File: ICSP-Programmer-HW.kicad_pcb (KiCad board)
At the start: 2 copper layers, 45 x 21 mm, 28 parts, among them J1 USB4105-GF-A-060, J2 61200621621, J3 Pins_2.54_1x2, U1 ATMEGA8A-MU, U2 FT230XQ, U3 74LVC1T45Z6, U4 74LVC1T45Z6, U5 74LVC1T45Z6, U6 74LVC1T45Z6, Y1 CSTNE16M0V530000R0

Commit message: Update readme
Add jumper to tie 5V to VCC
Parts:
- added JP1: SolderJumper2, Jumper:SolderJumper-2_P1.3mm_Open_RoundedPad1.0x1.5mm, F.Cu at (114.1, 120.9)
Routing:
- net /Target/TARGET_VCC: track 19.8 -> 40.5 mm
- net +5V: track 69.1 -> 71.3 mm
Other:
- board text added: "VCC"
- board text removed: "V+"

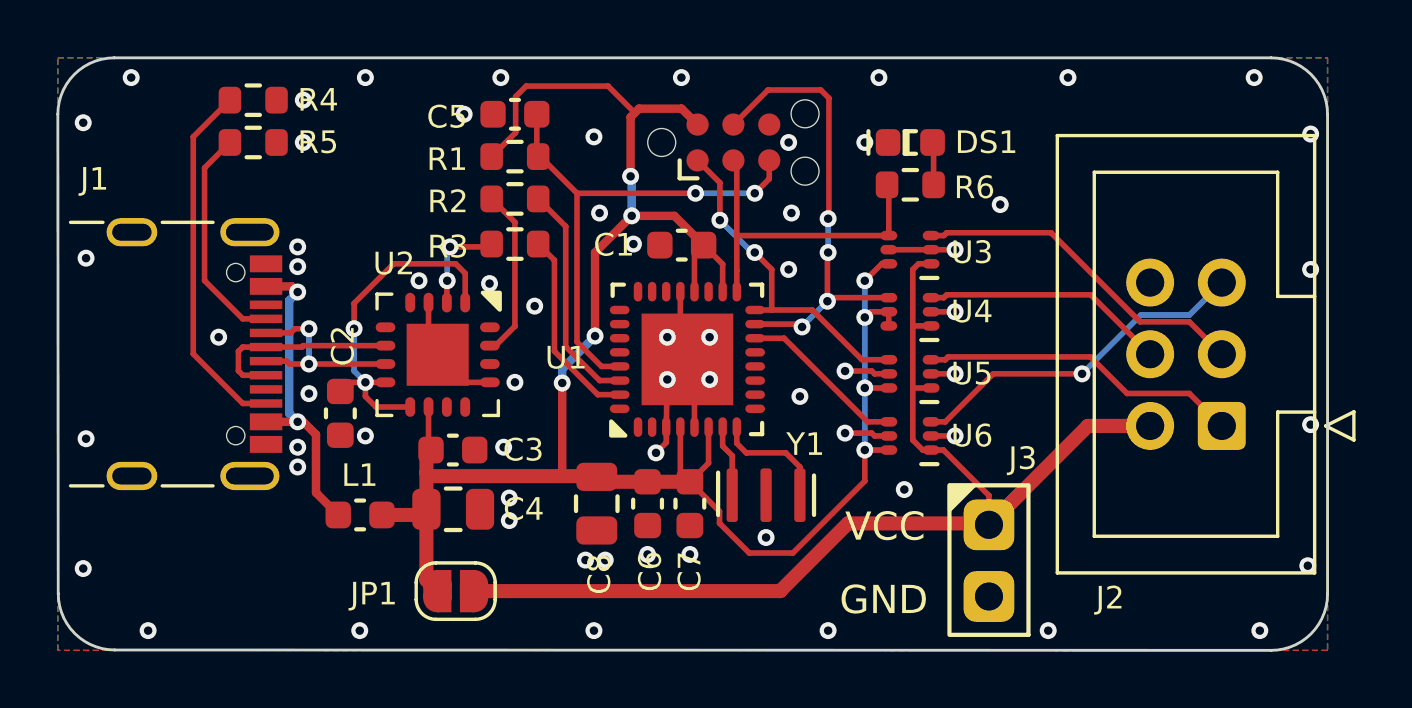
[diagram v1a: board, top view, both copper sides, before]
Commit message: Fix direction issue on MISO/MOSI
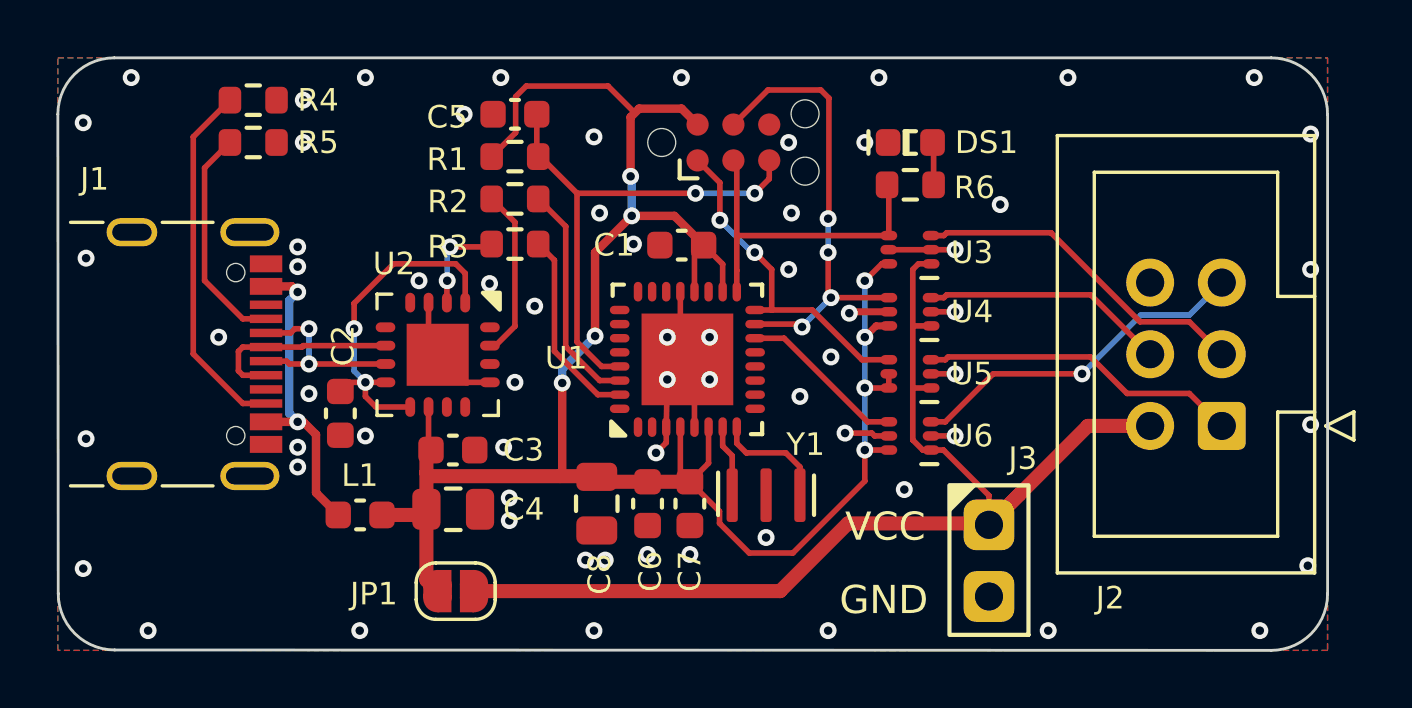
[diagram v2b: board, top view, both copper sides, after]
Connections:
- U4 pad 5: +5V -> GND
- U5 pad 5: GND -> +5V
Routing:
- net GND: track 16.7 -> 16.5 mm, vias 64 -> 65
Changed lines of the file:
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@@
       (net 20 "/MCU/ICSP_MOSI") (pinfunction "B") (pintype "bidirectional"))
     (pad "5" smd oval (at 0.75 0 180) (size 0.6 0.34) (layers "F.Cu" "F.Paste" "F.Mask")
-      (net 1 "+5V") (pinfunction "DIR") (pintype "input"))
+      (net 2 "GND") (pinfunction "DIR") (pintype "input"))
     (pad "6" smd oval (at 0.75 -0.5 180) (size 0.6 0.34) (layers "F.Cu" "F.Paste" "F.Mask")
       (net 1 "+5V") (pinfunction "VCCB") (pintype "power_in"))
@@
       (net 18 "/MCU/ICSP_MISO") (pinfunction "B") (pintype "bidirectional"))
     (pad "5" smd oval (at 0.75 0 180) (size 0.6 0.34) (layers "F.Cu" "F.Paste" "F.Mask")
-      (net 2 "GND") (pinfunction "DIR") (pintype "input"))
+      (net 1 "+5V") (pinfunction "DIR") (pintype "input"))
     (pad "6" smd oval (at 0.75 -0.5 180) (size 0.6 0.34) (layers "F.Cu" "F.Paste" "F.Mask")
       (net 1 "+5V") (pinfunction "VCCB") (pintype "power_in"))
@@
   (segment (start 123.45 118.075) (end 122.4 117.025) (width 0.2) (layer "F.Cu") (net 1))
   (segment (start 113.0625 118) (end 113.0625 116.7) (width 0.5) (layer "F.Cu") (net 1))
+  (segment (start 129.45 111.5) (end 128.999901 111.5) (width 0.25) (layer "F.Cu") (net 1))
   (segment (start 122.5625 110.2875) (end 122.5625 108.9625) (width 0.2) (layer "F.Cu") (net 1))
   (segment (start 128.6 115.9) (end 128.6 117) (width 0.2) (layer "F.Cu") (net 1))
@@
   (segment (start 124.505025 119.55) (end 123.45 118.494975) (width 0.2) (layer "F.Cu") (net 1))
   (segment (start 128.6 115.9) (end 129.45 115.9) (width 0.2) (layer "F.Cu") (net 1))
-  (segment (start 129.45 111) (end 129.45 111.5) (width 0.2) (layer "F.Cu") (net 1))
+  (segment (start 128.999901 111.5) (end 128.599901 111.9) (width 0.25) (layer "F.Cu") (net 1))
+  (segment (start 129.45 113.7) (end 129.45 113.2) (width 0.2) (layer "F.Cu") (net 1))
   (segment (start 126.05 119.55) (end 124.505025 119.55) (width 0.2) (layer "F.Cu") (net 1))
-  (segment (start 128.8 111) (end 128.6 111.2) (width 0.2) (layer "F.Cu") (net 1))
   (segment (start 123.5625 109.3125) (end 122.8875 108.6375) (width 0.2) (layer "F.Cu") (net 1))
   (segment (start 119.039597 108.899742) (end 120.339339 107.6) (width 0.3) (layer "F.Cu") (net 1))
@@
   (segment (start 120.6 103.8) (end 122.1075 103.8) (width 0.3) (layer "F.Cu") (net 1))
   (segment (start 111.4875 118.2) (end 112.8625 118.2) (width 0.5) (layer "F.Cu") (net 1))
-  (segment (start 129.45 111) (end 128.8 111) (width 0.2) (layer "F.Cu") (net 1))
   (segment (start 120.3 104.1) (end 120.6 103.8) (width 0.3) (layer "F.Cu") (net 1))
   (segment (start 123.5625 110.2875) (end 123.5625 109.3125) (width 0.2) (layer "F.Cu") (net 1))
@@
   (via (at 120.3 106.2) (size 0.6) (drill 0.3) (layers "F.Cu" "B.Cu") (net 1))
   (via (at 128.6 115.9) (size 0.6) (drill 0.3) (layers "F.Cu" "B.Cu") (net 1))
-  (via (at 128.6 111.2) (size 0.6) (drill 0.3) (layers "F.Cu" "B.Cu") (net 1))
+  (via (at 128.599901 111.9) (size 0.6) (drill 0.3) (layers "F.Cu" "B.Cu") (net 1))
   (via (at 128.599901 113.7) (size 0.6) (drill 0.3) (layers "F.Cu" "B.Cu") (net 1))
-  (segment (start 128.599901 113.7) (end 128.599901 111.200099) (width 0.2) (layer "B.Cu") (net 1))
+  (segment (start 128.6 111.899901) (end 128.6 109.9005) (width 0.2) (layer "B.Cu") (net 1))
+  (segment (start 128.599901 111.9) (end 128.6 111.899901) (width 0.2) (layer "B.Cu") (net 1))
   (segment (start 117.876089 113.023911) (end 119.039597 111.860403) (width 0.3) (layer "B.Cu") (net 1))
   (segment (start 117.876089 113.523911) (end 117.876089 113.023911) (width 0.3) (layer "B.Cu") (net 1))
+  (segment (start 128.599901 111.9) (end 128.599901 113.7) (width 0.2) (layer "B.Cu") (net 1))
   (segment (start 120.339339 107.6) (end 120.339339 106.239339) (width 0.3) (layer "B.Cu") (net 1))
   (segment (start 120.339339 106.239339) (end 120.3 106.2) (width 0.5) (layer "B.Cu") (net 1))
-  (segment (start 128.599901 111.200099) (end 128.6 111.2) (width 0.2) (layer "B.Cu") (net 1))
   (segment (start 128.599901 113.7) (end 128.599901 115.899901) (width 0.2) (layer "B.Cu") (net 1))
-  (segment (start 128.6 109.9005) (end 128.6 111.2) (width 0.2) (layer "B.Cu") (net 1))
   (segment (start 128.599901 115.899901) (end 128.6 115.9) (width 0.2) (layer "B.Cu") (net 1))
   (segment (start 122.0625 111.3125) (end 121.5 111.875) (width 0.2) (layer "F.Cu") (net 2))
   (segment (start 129.45 115.4) (end 128.948529 115.4) (width 0.2) (layer "F.Cu") (net 2))
   (segment (start 128.948529 115.4) (end 128.848529 115.3) (width 0.2) (layer "F.Cu") (net 2))
+  (segment (start 128.1 111) (end 129.45 111) (width 0.25) (layer "F.Cu") (net 2))
   (segment (start 128.848529 115.3) (end 127.9 115.3) (width 0.2) (layer "F.Cu") (net 2))
   (segment (start 121.6 113.4) (end 121.5625 113.5625) (width 0.2) (layer "F.Cu") (net 2))
-  (segment (start 128.94843 113.2) (end 129.45 113.2) (width 0.2) (layer "F.Cu") (net 2))
   (segment (start 121.5625 115.0875) (end 121.6 113.4) (width 0.2) (layer "F.Cu") (net 2))
   (segment (start 122.5625 115.0875) (end 122.5625 114.0625) (width 0.2) (layer "F.Cu") (net 2))
@@
   (segment (start 130.95 113.2) (end 131.8 113.2) (width 0.2) (layer "F.Cu") (net 2))
   (segment (start 114.4375 113.5) (end 114.0125 113.075) (width 0.2) (layer "F.Cu") (net 2))
-  (segment (start 128.84843 113.1) (end 128.94843 113.2) (width 0.2) (layer "F.Cu") (net 2))
   (segment (start 113.1375 111.75) (end 112.9125 111.975) (width 0.2) (layer "F.Cu") (net 2))
   (segment (start 129.45 108.8) (end 130.95 108.8) (width 0.2) (layer "F.Cu") (net 2))
   (segment (start 121.2 116) (end 121.5625 115.6375) (width 0.2) (layer "F.Cu") (net 2))
-  (segment (start 127.9 113.1) (end 128.84843 113.1) (width 0.2) (layer "F.Cu") (net 2))
+  (segment (start 128.0505 111.0495) (end 128.1 111) (width 0.25) (layer "F.Cu") (net 2))
   (segment (start 121.5625 115.6375) (end 121.5625 115.0875) (width 0.2) (layer "F.Cu") (net 2))
   (segment (start 130.95 108.8) (end 131.8 108.8) (width 0.2) (layer "F.Cu") (net 2))
@@
   (via (at 116 117.6) (size 0.6) (drill 0.3) (layers "F.Cu" "B.Cu") (free) (net 2))
   (via (at 108.7 105) (size 0.6) (drill 0.3) (layers "F.Cu" "B.Cu") (free) (net 2))
-  (via (at 127.9 113.1) (size 0.6) (drill 0.3) (layers "F.Cu" "B.Cu") (free) (net 2))
+  (via (at 127.4 112.6) (size 0.6) (drill 0.3) (layers "F.Cu" "B.Cu") (free) (net 2))
   (via (at 118.7 119.8) (size 0.6) (drill 0.3) (layers "F.Cu" "B.Cu") (free) (net 2))
   (via (at 135.1 122.3) (size 0.6) (drill 0.3) (layers "F.Cu" "B.Cu") (free) (net 2))
@@
   (via (at 101 109.1) (size 0.6) (drill 0.3) (layers "F.Cu" "B.Cu") (free) (net 2))
   (via (at 115.3 110) (size 0.6) (drill 0.3) (layers "F.Cu" "B.Cu") (free) (net 2))
+  (via (at 128.0505 111.0495) (size 0.6) (drill 0.3) (layers "F.Cu" "B.Cu") (free) (net 2))
   (via (at 126.3 114) (size 0.6) (drill 0.3) (layers "F.Cu" "B.Cu") (free) (net 2))
   (via (at 119.2 107.5) (size 0.6) (drill 0.3) (layers "F.Cu" "B.Cu") (free) (net 2))
@@
   (segment (start 124.0625 110.2875) (end 124.0625 109.5375) (width 0.2) (layer "F.Cu") (net 19))
   (segment (start 127.4 110.5) (end 129.45 110.5) (width 0.2) (layer "F.Cu") (net 20))
-  (segment (start 127.273911 108.926089) (end 127.3 108.9) (width 0.2) (layer "F.Cu") (net 20))
   (segment (start 126.276589 111.4375) (end 126.376089 111.537) (width 0.2) (layer "F.Cu") (net 20))
   (segment (start 127.3278 103.4278) (end 127.0387 103.1387) (width 0.2) (layer "F.Cu") (net 20))
+  (segment (start 127.3 110.4) (end 127.3 108.9) (width 0.2) (layer "F.Cu") (net 20))
   (segment (start 125.1688 103.1387) (end 123.9425 104.365) (width 0.2) (layer "F.Cu") (net 20))
   (segment (start 124.7125 111.4375) (end 126.276589 111.4375) (width 0.2) (layer "F.Cu") (net 20))
   (segment (start 127.3 107.7005) (end 127.3278 107.6727) (width 0.2) (layer "F.Cu") (net 20))
   (segment (start 127.0387 103.1387) (end 125.1688 103.1387) (width 0.2) (layer "F.Cu") (net 20))
+  (segment (start 127.4 110.5) (end 127.3 110.4) (width 0.2) (layer "F.Cu") (net 20))
   (segment (start 127.3278 107.6727) (end 127.3278 103.4278) (width 0.2) (layer "F.Cu") (net 20))
-  (segment (start 127.273911 110.626089) (end 127.273911 108.926089) (width 0.2) (layer "F.Cu") (net 20))
-  (segment (start 127.273911 110.626089) (end 127.4 110.5) (width 0.2) (layer "F.Cu") (net 20))
-  (via (at 127.273911 110.626089) (size 0.6) (drill 0.3) (layers "F.Cu" "B.Cu") (net 20))
+  (via (at 127.4 110.5) (size 0.6) (drill 0.3) (layers "F.Cu" "B.Cu") (net 20))
   (via (at 127.3 107.7005) (size 0.6) (drill 0.3) (layers "F.Cu" "B.Cu") (net 20))
   (via (at 126.376089 111.537) (size 0.6) (drill 0.3) (layers "F.Cu" "B.Cu") (net 20))
   (via (at 127.3 108.9) (size 0.6) (drill 0.3) (layers "F.Cu" "B.Cu") (net 20))
-  (segment (start 126.376089 111.523911) (end 127.273911 110.626089) (width 0.2) (layer "B.Cu") (net 20))
-  (segment (start 126.376089 111.537) (end 126.376089 111.523911) (width 0.2) (layer "B.Cu") (net 20))
+  (segment (start 127.4 110.5) (end 126.376089 111.523911) (width 0.2) (layer "B.Cu") (net 20))
+  (segment (start 126.376089 111.523911) (end 126.376089 111.537) (width 0.2) (layer "B.Cu") (net 20))
   (segment (start 127.3 108.9) (end 127.3 107.7005) (width 0.2) (layer "B.Cu") (net 20))
   (segment (start 116.2 107.825) (end 115.375 107) (width 0.2) (layer "F.Cu") (net 21))

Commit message: PCB version to 1.1
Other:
- board text added: "ICSP-Programmer v1.1 Jul 23"
- board text removed: "ICSP-Programmer v1.0 Jul 23"
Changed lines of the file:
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@@
   (gr_arc (start 100 104) (mid 100.585786 102.585786) (end 102 102)
     (stroke (width 0.1) (type default)) (layer "Edge.Cuts"))
-  (gr_text "ICSP-Programmer\nv1.0\nJul 23" (at 136 111.8) (layer "B.SilkS")
+  (gr_text "ICSP-Programmer\nv1.1\nJul 23" (at 136 111.8) (layer "B.SilkS")
     (effects (font (size 1 1) (thickness 0.15)) (justify left bottom mirror))
   )
